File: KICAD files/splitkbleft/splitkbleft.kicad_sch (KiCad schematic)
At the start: 71 parts, among them SW1 SW_Push, SW10 SW_Push, SW11 SW_Push, SW12 SW_Push, SW13 SW_Push, SW14 SW_Push, SW15 SW_Push, SW16 SW_Push, SW17 SW_Push, SW18 SW_Push, SW19 SW_Push, SW2 SW_Push, SW20 SW_Push, SW21 SW_Push, SW22 SW_Push, SW23 SW_Push, SW24 SW_Push, SW25 SW_Push, SW26 SW_Push, SW27 SW_Push, SW28 SW_Push, SW29 SW_Push, SW3 SW_Push, SW30 SW_Push, SW33 SW_Push, SW34 SW_Push, SW35 SW_Push, SW36 SW_Push, SW4 SW_Push, SW5 SW_Push, SW6 SW_Push, SW7 SW_Push, SW8 SW_Push, SW9 SW_Push, U2 nice_nano

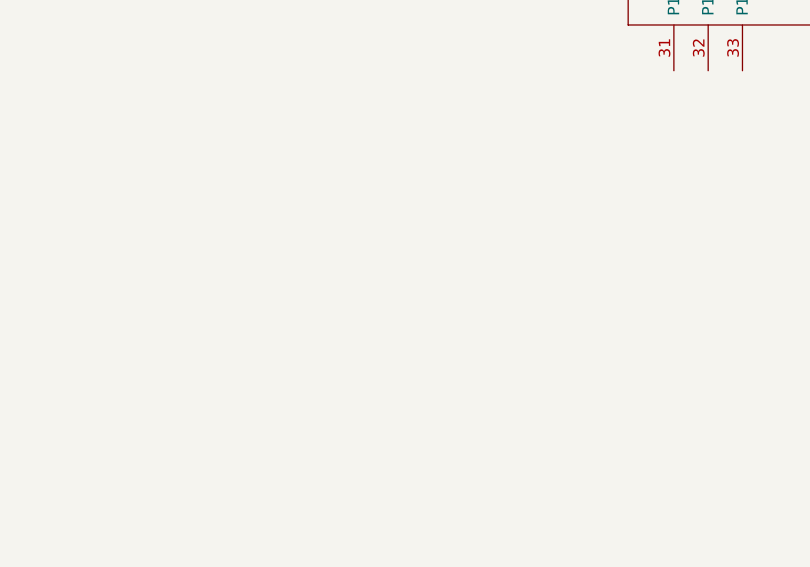
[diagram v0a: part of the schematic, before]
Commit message: Edited PCBs
- Added mounting holes to both pcbs and schematics
- Changed the shape and size of both PCBs
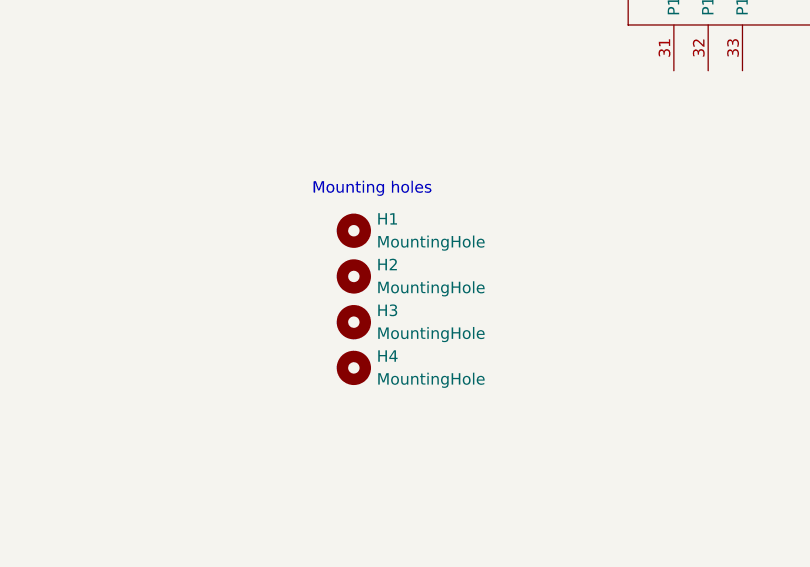
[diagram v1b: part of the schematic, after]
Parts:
- added H1, H2, H3, H4: MountingHole, symbol Mechanical:MountingHole
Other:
- note added: "Mounting holes"
